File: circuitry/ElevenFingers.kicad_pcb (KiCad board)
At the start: 2 copper layers, 154.1 x 152.9 mm, 95 parts, among them J1 OLED, SW1 MX, SW10 MX, SW11 MX, SW12 MX, SW13 MX, SW14 MX, SW15 MX, SW16 MX, SW17 MX, SW18 MX, SW19 MX, SW2 MX, SW20 MX, SW21 MX, SW22 MX, SW23 MX, SW24 MX, SW25 MX, SW26 MX, SW27 MX, SW28 MX, SW29 MX, SW3 MX, SW30 MX, SW4 MX, SW5 MX, SW6 MX, SW7 MX, SW8 MX, SW9 MX, U1 ProMicro, U2 TRRS

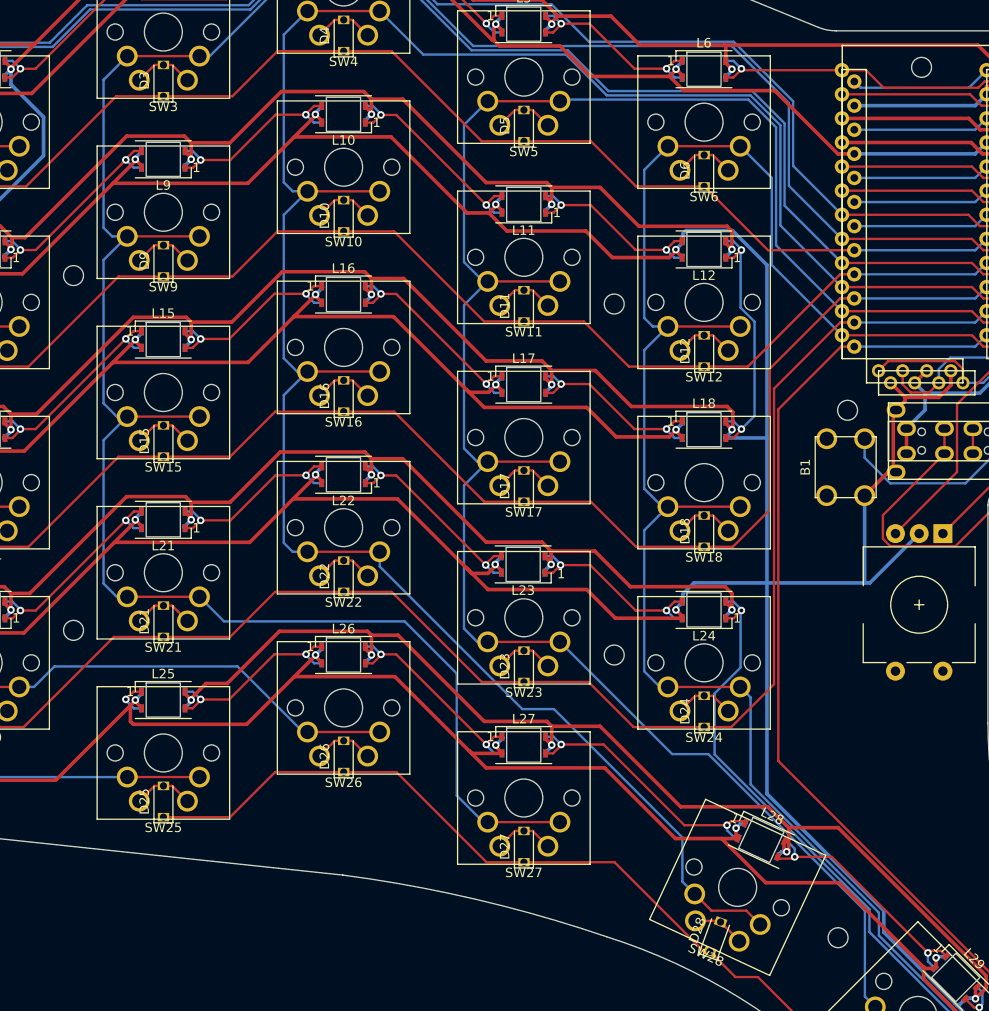
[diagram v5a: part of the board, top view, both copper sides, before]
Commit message: changed pcb holes to NPTH, mechanical, generated case dxf files
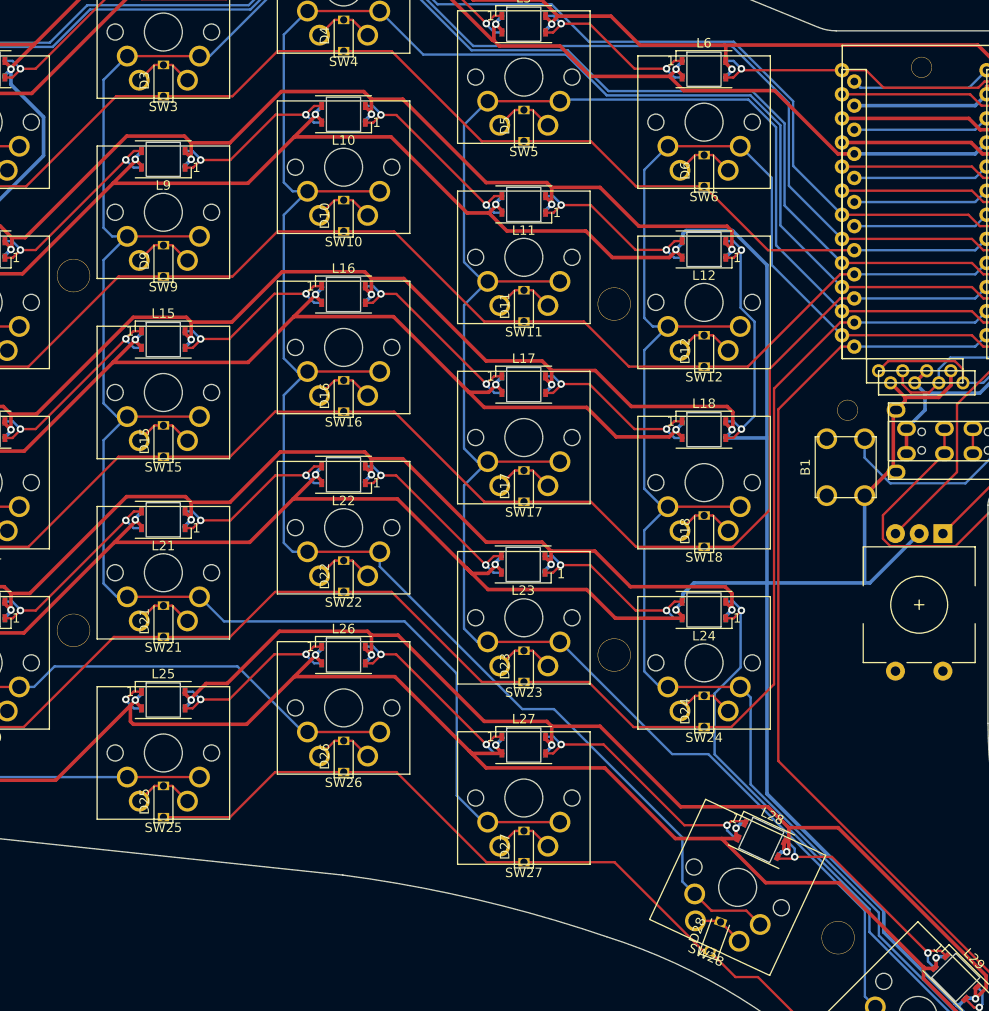
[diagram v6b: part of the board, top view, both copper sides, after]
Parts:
- added ?: , , F.Cu at (251.0, 105.0)
- added ?: , , F.Cu at (175.0, 71.0)
- added ?: , , F.Cu at (250.0, 86.0)
- added ?: , , F.Cu at (67.0, 126.0)
- added ?: , , F.Cu at (251.0, 95.0)
- added REF**: hole_m2screw, ElevenFingers:hole_m2screw, F.Cu at (174.0, 71.0)
- added REF**: hole_m2spacer, ElevenFingers:hole_m2spacer, F.Cu at (66.0, 94.0)
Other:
- outline, holes or cut-outs redrawn
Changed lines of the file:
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@@
     (pad_to_mask_clearance 0)
     (pcbplotparams
-      (layerselection 0x00010fc_ffffffff)
+      (layerselection 0x00010f0_ffffffff)
       (disableapertmacros false)
       (usegerberextensions false)
@@
       (hpglpenspeed 20)
       (hpglpendiameter 15.000000)
-      (dxfpolygonmode true)
-      (dxfimperialunits true)
+      (dxfpolygonmode false)
+      (dxfimperialunits false)
       (dxfusepcbnewfont true)
       (psnegative false)
@@
       (outputformat 1)
       (mirror false)
-      (drillshape 1)
+      (drillshape 0)
       (scaleselection 1)
-      (outputdirectory "")
+      (outputdirectory "gerbers-pcb/")
     )
   )
@@
     )
   )
+  (footprint "" (layer "F.Cu")
+    (at 251 105)
+    (fp_text reference "" (at 0 0) (layer "F.SilkS")
+      (effects (font (size 1.27 1.27) (thickness 0.15)))
+    )
+    (fp_text value "" (at 0 0) (layer "F.SilkS")
+      (effects (font (size 1.27 1.27) (thickness 0.15)))
+    )
+    (pad "" np_thru_hole circle (at -103.8 55.6) (size 3.5 3.5) (drill 3.4) (layers F&B.Cu *.Mask))
+  )
   (footprint "ElevenFingers:LED_SK6812MINI_PLCC4_3.5x3.5mm_P1.75mm" (layer "F.Cu")
     (at 114.061846 140.296051)
@@
     )
   )
+  (footprint "" (layer "F.Cu")
+    (at 175 71)
+    (fp_text reference "" (at 0 0) (layer "F.SilkS")
+      (effects (font (size 1.27 1.27) (thickness 0.15)))
+    )
+    (fp_text value "" (at 0 0) (layer "F.SilkS")
+      (effects (font (size 1.27 1.27) (thickness 0.15)))
+    )
+    (pad "" np_thru_hole circle (at -26.8 34) (size 2.2 2.2) (drill 2.1) (layers F&B.Cu *.Mask))
+  )
   (footprint "ElevenFingers:LED_SK6812MINI_PLCC4_3.5x3.5mm_P1.75mm" (layer "F.Cu")
     (at 95.061846 130.796051)
@@
     )
   )
+  (footprint "ElevenFingers:hole_m2screw" (layer "F.Cu")
+    (at 174 71)
+    (attr through_hole)
+    (fp_text reference "REF**" (at 0 -0.5 unlocked) (layer "F.SilkS") hide
+      (effects (font (size 1 1) (thickness 0.15)))
+    )
+    (fp_text value "hole_m2screw" (at 0 1 unlocked) (layer "F.Fab") hide
+      (effects (font (size 1 1) (thickness 0.15)))
+    )
+    (fp_text user "${REFERENCE}" (at 0 2.5 unlocked) (layer "F.Fab") hide
+      (effects (font (size 1 1) (thickness 0.15)))
+    )
+    (pad "" np_thru_hole circle (at -18 -2.15) (size 2.2 2.2) (drill 2.1) (layers F&B.Cu *.Mask))
+  )
   (footprint "ElevenFingers:D_SOD-123" (layer "F.Cu")
     (at 95.081846 122.496051 90)
@@
     )
   )
+  (footprint "" (layer "F.Cu")
+    (at 250 86)
+    (fp_text reference "" (at 0 0) (layer "F.SilkS")
+      (effects (font (size 1.27 1.27) (thickness 0.15)))
+    )
+    (fp_text value "" (at 0 0) (layer "F.SilkS")
+      (effects (font (size 1.27 1.27) (thickness 0.15)))
+    )
+    (pad "" np_thru_hole circle (at -126.4 7.8) (size 3.5 3.5) (drill 3.4) (layers F&B.Cu *.Mask))
+  )
   (footprint "ElevenFingers:LED_SK6812MINI_PLCC4_3.5x3.5mm_P1.75mm" (layer "F.Cu")
     (at 133.061846 69.046051)
@@
     )
   )
+  (footprint "" (layer "F.Cu")
+    (at 67 126)
+    (fp_text reference "" (at 0 0) (layer "F.SilkS")
+      (effects (font (size 1.27 1.27) (thickness 0.15)))
+    )
+    (fp_text value "" (at 0 0) (layer "F.SilkS")
+      (effects (font (size 1.27 1.27) (thickness 0.15)))
+    )
+    (pad "" np_thru_hole circle (at -0.4 2.2) (size 3.5 3.5) (drill 3.4) (layers F&B.Cu *.Mask))
+  )
   (footprint "ElevenFingers:D_SOD-123" (layer "F.Cu")
     (at 57.081846 136.746051 90)
@@
     )
   )
+  (footprint "" (layer "F.Cu")
+    (at 251 95)
+    (fp_text reference "" (at 0 0) (layer "F.SilkS")
+      (effects (font (size 1.27 1.27) (thickness 0.15)))
+    )
+    (fp_text value "" (at 0 0) (layer "F.SilkS")
+      (effects (font (size 1.27 1.27) (thickness 0.15)))
+    )
+    (pad "" np_thru_hole circle (at -127.4 35.8) (size 3.5 3.5) (drill 3.4) (layers F&B.Cu *.Mask))
+  )
   (footprint "ElevenFingers:D_SOD-123" (layer "F.Cu")
     (at 38.081846 103.496051 90)
@@
     )
   )
+  (footprint "ElevenFingers:hole_m2spacer" (layer "F.Cu")
+    (at 66 94)
+    (attr through_hole)
+    (fp_text reference "REF**" (at 0 -0.5 unlocked) (layer "F.SilkS") hide
+      (effects (font (size 1 1) (thickness 0.15)))
+    )
+    (fp_text value "hole_m2spacer" (at 0 2 unlocked) (layer "F.Fab") hide
+      (effects (font (size 1 1) (thickness 0.15)))
+    )
+    (fp_text user "${REFERENCE}" (at 0 3 unlocked) (layer "F.Fab") hide
+      (effects (font (size 1 1) (thickness 0.15)))
+    )
+    (pad "" np_thru_hole circle (at 0.6 -3.2) (size 3.5 3.5) (drill 3.4) (layers F&B.Cu *.Mask))
+  )
   (footprint "ElevenFingers:SW_Cherry_MX_1.00u_PCB" (layer "F.Cu")
     (at 116.611846 83.796051)
@@
   )
   (gr_arc (start 181.923305 191.349785) (mid 182 192.4) (end 181.260639 193.149785) (layer "Edge.Cuts") (width 0.1))
-  (gr_circle (center 123.6 93.8) (end 124.65 93.8) (layer "Edge.Cuts") (width 0.1) (fill none))
   (gr_line (start 168 161) (end 181.923305 191.349785) (layer "Edge.Cuts") (width 0.1))
   (gr_arc (start 28.9 147) (mid 28.261992 146.669207) (end 28 146) (layer "Edge.Cuts") (width 0.1))
@@
   (gr_line (start 29.3 67.6) (end 85.1 48.212461) (layer "Edge.Cuts") (width 0.1))
   (gr_arc (start 122.8 160.5) (mid 144.677053 172.690425) (end 160 192.5) (layer "Edge.Cuts") (width 0.1))
-  (gr_circle (center 66.6 128.2) (end 67.65 128.2) (layer "Edge.Cuts") (width 0.1) (fill none))
   (gr_line (start 147 65) (end 165 65) (layer "Edge.Cuts") (width 0.1))
-  (gr_circle (center 123.6 130.8) (end 124.65 130.8) (layer "Edge.Cuts") (width 0.1) (fill none))
   (gr_arc (start 147 65) (mid 146.054462 64.909782) (end 145.143047 64.642383) (layer "Edge.Cuts") (width 0.1))
   (gr_line (start 160 192.5) (end 163.553554 200.239341) (layer "Edge.Cuts") (width 0.1))
@@
   (gr_arc (start 167 111) (mid 166.414214 112.414214) (end 165 113) (layer "Edge.Cuts") (width 0.1))
   (gr_line (start 28 69.457249) (end 28 146) (layer "Edge.Cuts") (width 0.1))
-  (gr_circle (center 66.6 90.8) (end 67.65 90.8) (layer "Edge.Cuts") (width 0.1) (fill none))
   (gr_line (start 165.053553 200.73934) (end 181.260639 193.149785) (layer "Edge.Cuts") (width 0.1))
   (gr_arc (start 165 65) (mid 166.414214 65.585786) (end 167 67) (layer "Edge.Cuts") (width 0.1))
-  (gr_circle (center 148.2 105) (end 149.25 105) (layer "Edge.Cuts") (width 0.1) (fill none))
   (gr_arc (start 163 115) (mid 163.585786 113.585786) (end 165 113) (layer "Edge.Cuts") (width 0.1))
-  (gr_circle (center 147.2 160.6) (end 148.25 160.6) (layer "Edge.Cuts") (width 0.1) (fill none))
   (gr_arc (start 104 48) (mid 104.356862 48.032025) (end 104.702247 48.127342) (layer "Edge.Cuts") (width 0.1))
   (gr_arc (start 95 154) (mid 109.060373 156.564097) (end 122.8 160.5) (layer "Edge.Cuts") (width 0.1))
@@
   (gr_line (start 167 111) (end 167 67) (layer "Edge.Cuts") (width 0.1))
   (gr_line (start 104.702247 48.127342) (end 145.143047 64.642383) (layer "Edge.Cuts") (width 0.1))
-  (gr_circle (center 156 68.85) (end 157.05 68.85) (layer "Edge.Cuts") (width 0.1) (fill none))
   (gr_line (start 27 148.199999) (end 95 155) (layer "User.1") (width 0.15))
   (gr_line (start 168 202) (end 180.981869 195.966527) (layer "User.1") (width 0.15))
@@
   (gr_circle (center 123.6 130.8) (end 124.65 130.8) (layer "User.4") (width 0.1) (fill none))
   (gr_arc (start 167 58) (mid 169.12132 58.87868) (end 170 61) (layer "User.4") (width 0.1))
-  (gr_arc (start 148 58) (mid 146.071288 57.684164) (end 144.256953 56.957617) (layer "User.4") (width 0.1))
+  (gr_arc (start 149 58) (mid 146.567123 57.757967) (end 144.256953 56.957617) (layer "User.4") (width 0.1))
   (gr_circle (center 24 145) (end 25.05 145) (layer "User.4") (width 0.1) (fill none))
   (gr_circle (center 156 68.85) (end 157.05 68.85) (layer "User.4") (width 0.1) (fill none))
@@
   (gr_circle (center 123.6 93.8) (end 124.65 93.8) (layer "User.4") (width 0.1) (fill none))
   (gr_line (start 174.919174 158.699958) (end 189.080826 189.300042) (layer "User.4") (width 0.1))
+  (gr_circle (center 166.95 61) (end 168 61) (layer "User.4") (width 0.1) (fill none))
   (gr_line (start 27.6 154) (end 94 161) (layer "User.4") (width 0.1))
   (gr_arc (start 167.881333 208.45) (mid 161.302331 209.220085) (end 156 205.25) (layer "User.4") (width 0.1))
-  (gr_line (start 148 58) (end 167 58) (layer "User.4") (width 0.1))
+  (gr_line (start 149 58) (end 167 58) (layer "User.4") (width 0.1))
   (gr_line (start 167.881333 208.45) (end 186.118668 199.550001) (layer "User.4") (width 0.1))
   (gr_circle (center 95 44.05) (end 96.05 44.05) (layer "User.4") (width 0.1) (fill none))
